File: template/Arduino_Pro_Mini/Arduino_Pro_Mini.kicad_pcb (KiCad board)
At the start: 2 copper layers, 17.8 x 33 mm, 5 parts, among them P1 Digital, P2 COM, P3 ADC, P4 Analog, P5 ADC

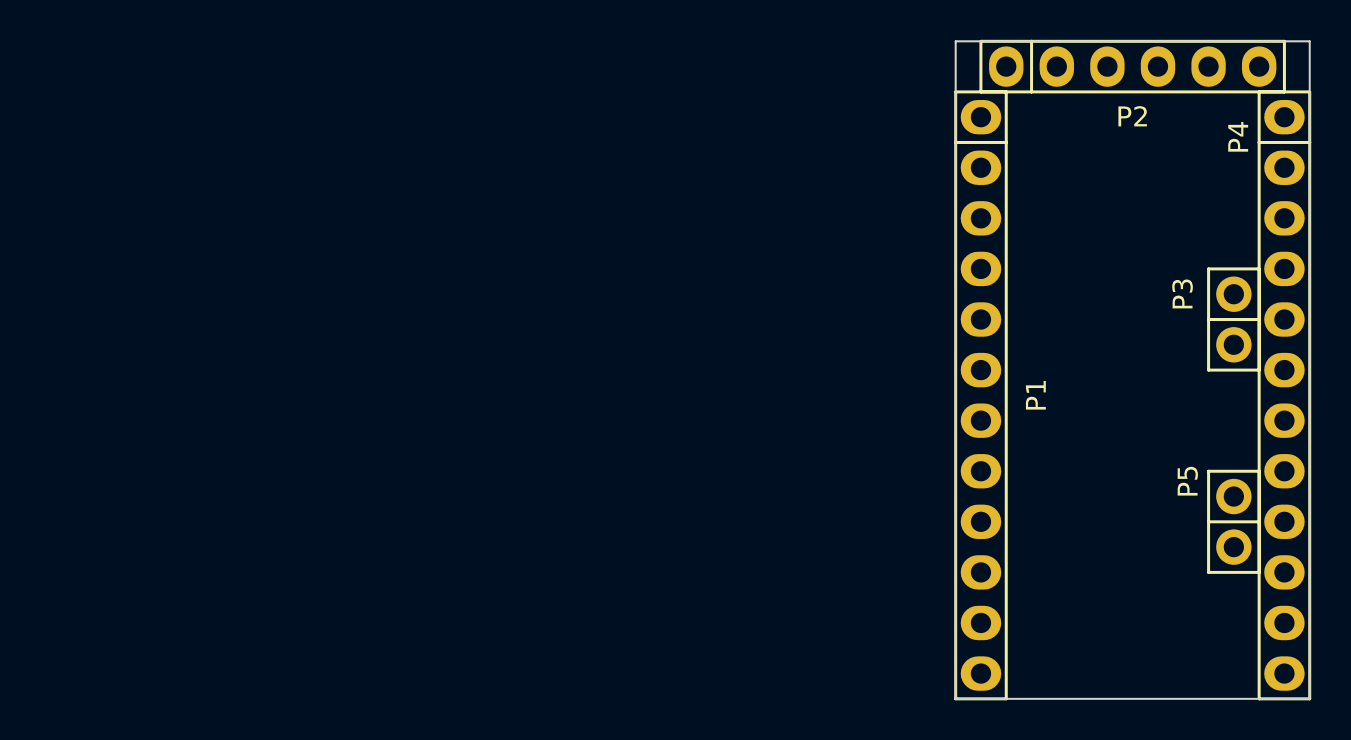
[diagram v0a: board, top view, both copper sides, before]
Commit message: fix: change original libs; add: new components
- Fix LIS3DH pins positions;
- Add ATmega164P symbol;
- Add 3D model to the L_Wuerth_HCM-7050;
- Add parameters for R_RES (Assembly...).
- Add parameters for R_RES and C_CAP;
- Fix SOIC-8 package 3D model;
- Add new parameters for many symbols;
- Change text height from 70 mil to 50 mil;
- Add solder mask expansion for 2-contact jumpers;
- Change thermopad vias of QFN-20-1EP_3x3mm_P0.45mm_EP1.6x1.6mm_ThermalVias;
- Add D_SMAF footprint;
- Fillet silk for C_1206;
-Rectangle silk for R_1206;
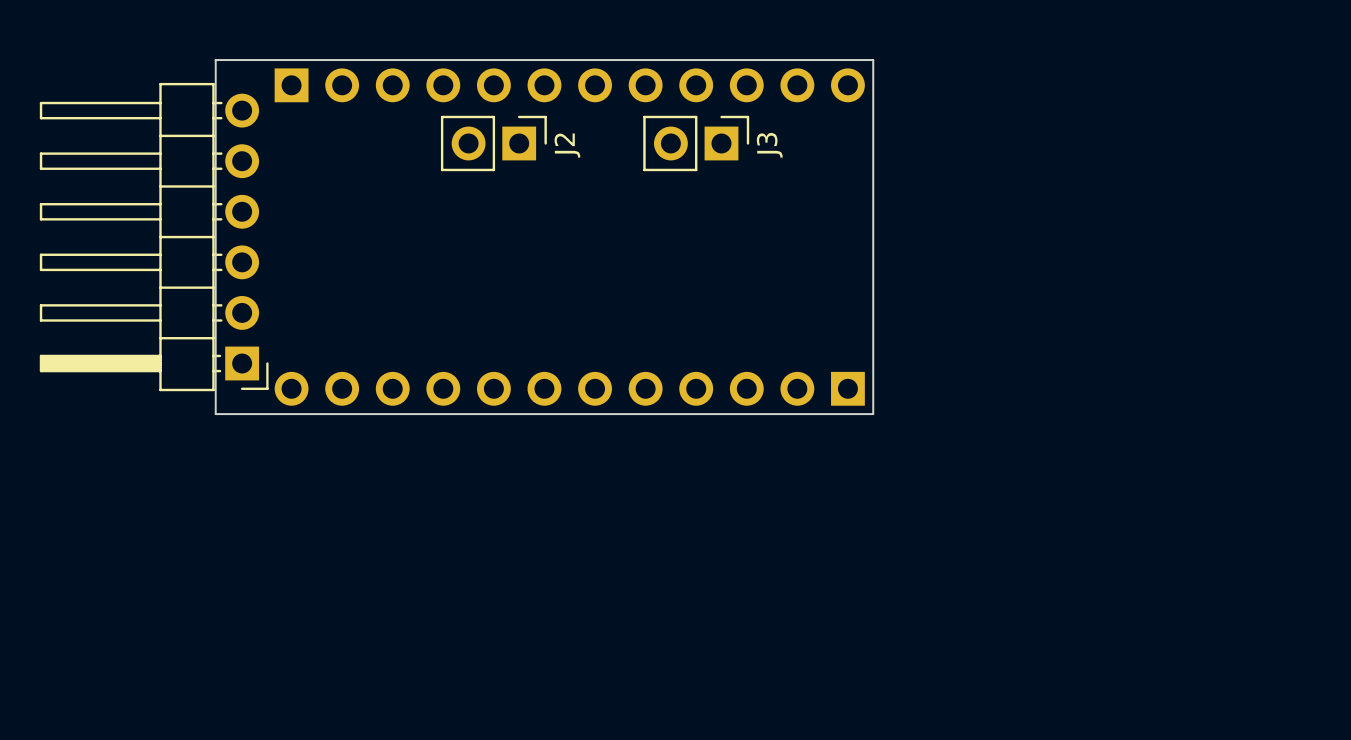
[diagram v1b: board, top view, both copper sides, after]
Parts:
- removed P1: Digital, Socket_Arduino_Pro_Mini:Socket_Strip_Arduino_1x12
- removed P2: COM, Socket_Arduino_Pro_Mini:Socket_Strip_Arduino_1x06
- removed P3, P5: ADC, Socket_Arduino_Pro_Mini:Socket_Strip_Arduino_1x02
- removed P4: Analog, Socket_Arduino_Pro_Mini:Socket_Strip_Arduino_1x12
- added J1: FTDI, Connector_PinHeader_2.54mm:PinHeader_1x06_P2.54mm_Horizontal, F.Cu at (101.3, 97.5)
- added J2: I2C, Connector_PinHeader_2.54mm:PinHeader_1x02_P2.54mm_Vertical, F.Cu at (115.2, 86.4)
- added J3: Analog, Connector_PinHeader_2.54mm:PinHeader_1x02_P2.54mm_Vertical, F.Cu at (125.4, 86.4)
- added J6: Digital, Connector_PinHeader_2.54mm:PinHeader_1x12_P2.54mm_Vertical, B.Cu at (103.8, 83.5)
- added J7: Analog, Connector_PinHeader_2.54mm:PinHeader_1x12_P2.54mm_Vertical, B.Cu at (131.8, 98.7)
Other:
- board size 17.8 x 33 mm -> 33 x 17.8 mm
- board text removed: "1"
